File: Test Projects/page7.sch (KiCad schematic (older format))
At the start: 22 parts, among them P2 CONN_01X03, P30 CONN_01X03, U31 SGTL5000, U5 SGTL5000

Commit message: Post review with Byron
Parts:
- added P38, P39: CONN_01X05, Pin_Headers:Pin_Header_Straight_1x05, symbol CONN_01X05
- C10, C11, C12, C13, C14, C37, C38, C39, C40, C41: footprint Capacitors_SMD:C_1206 -> Capacitors_SMD:C_0603
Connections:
- net GND: now also U31.33 (GND), U5.33 (GND), P38.1 (P1), P39.1 (P1)
- net at U5.11 (LINEOUTR): now also P38.4 (P4)
- net at U5.12 (LINEOUTL): now also P38.5 (P5)
- net at U5.13 (LINEINR): now also P38.3 (P3)
- net at U5.14 (LINEINL): now also P38.2 (P2)
- net at U31.11 (LINEOUTR): now also P39.4 (P4)
- net at U31.12 (LINEOUTL): now also P39.5 (P5)
- net at U31.13 (LINEINR): now also P39.3 (P3)
- net at U31.14 (LINEINL): now also P39.2 (P2)

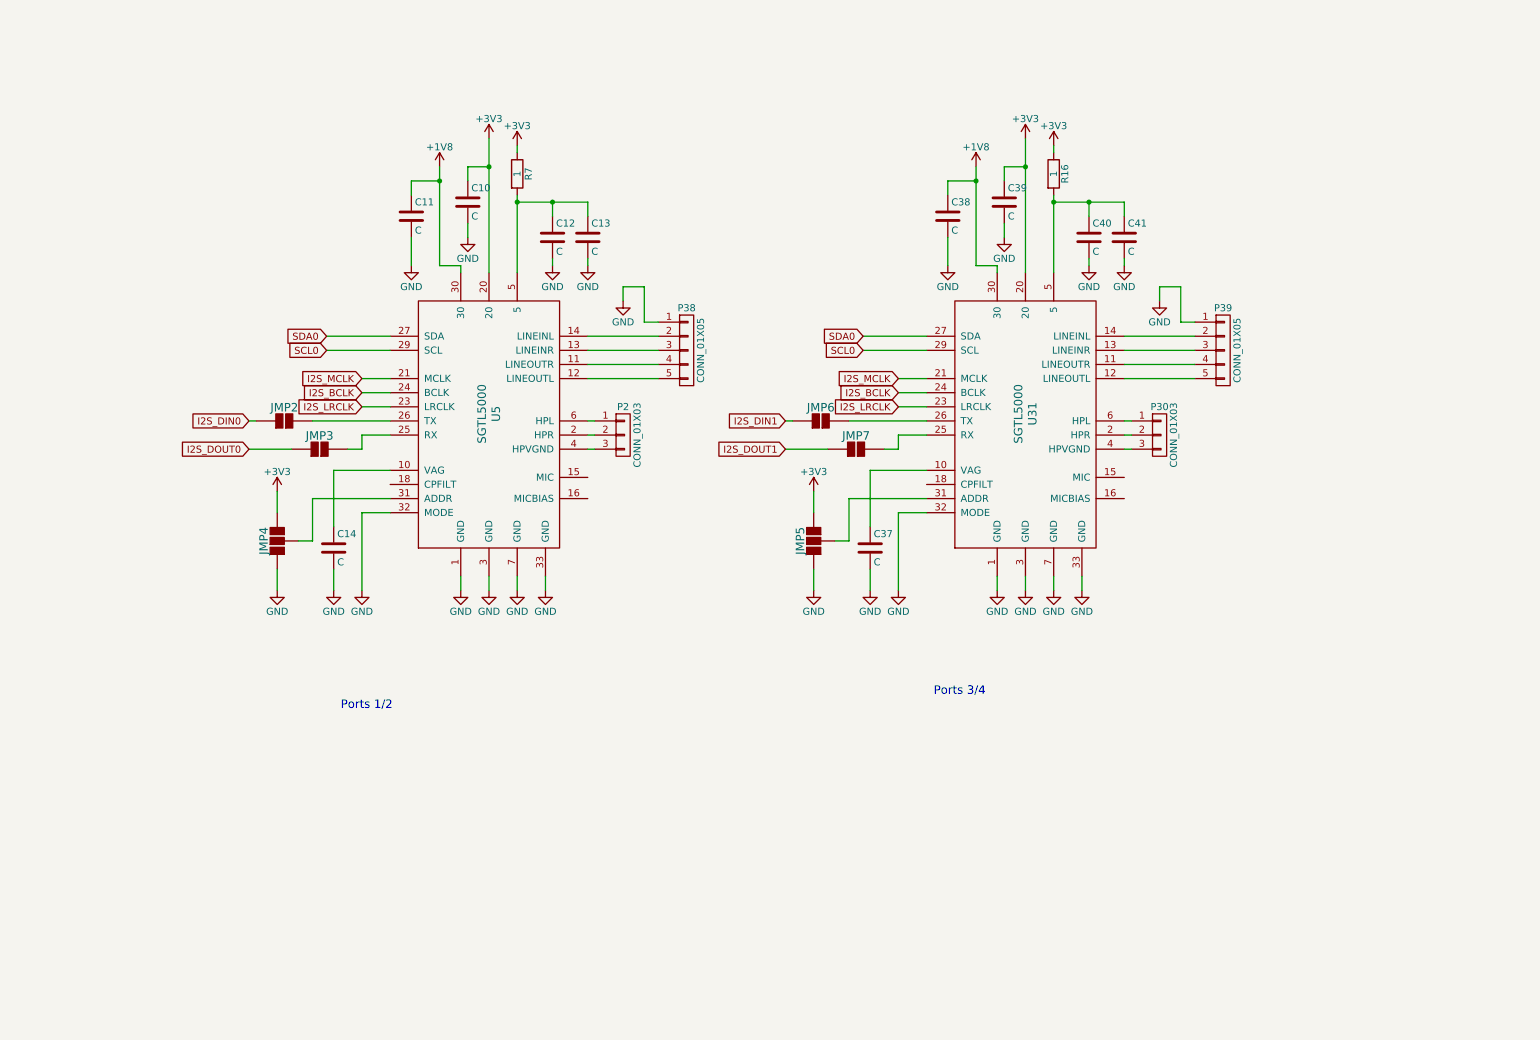
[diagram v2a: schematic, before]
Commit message: Added holes, moved layout
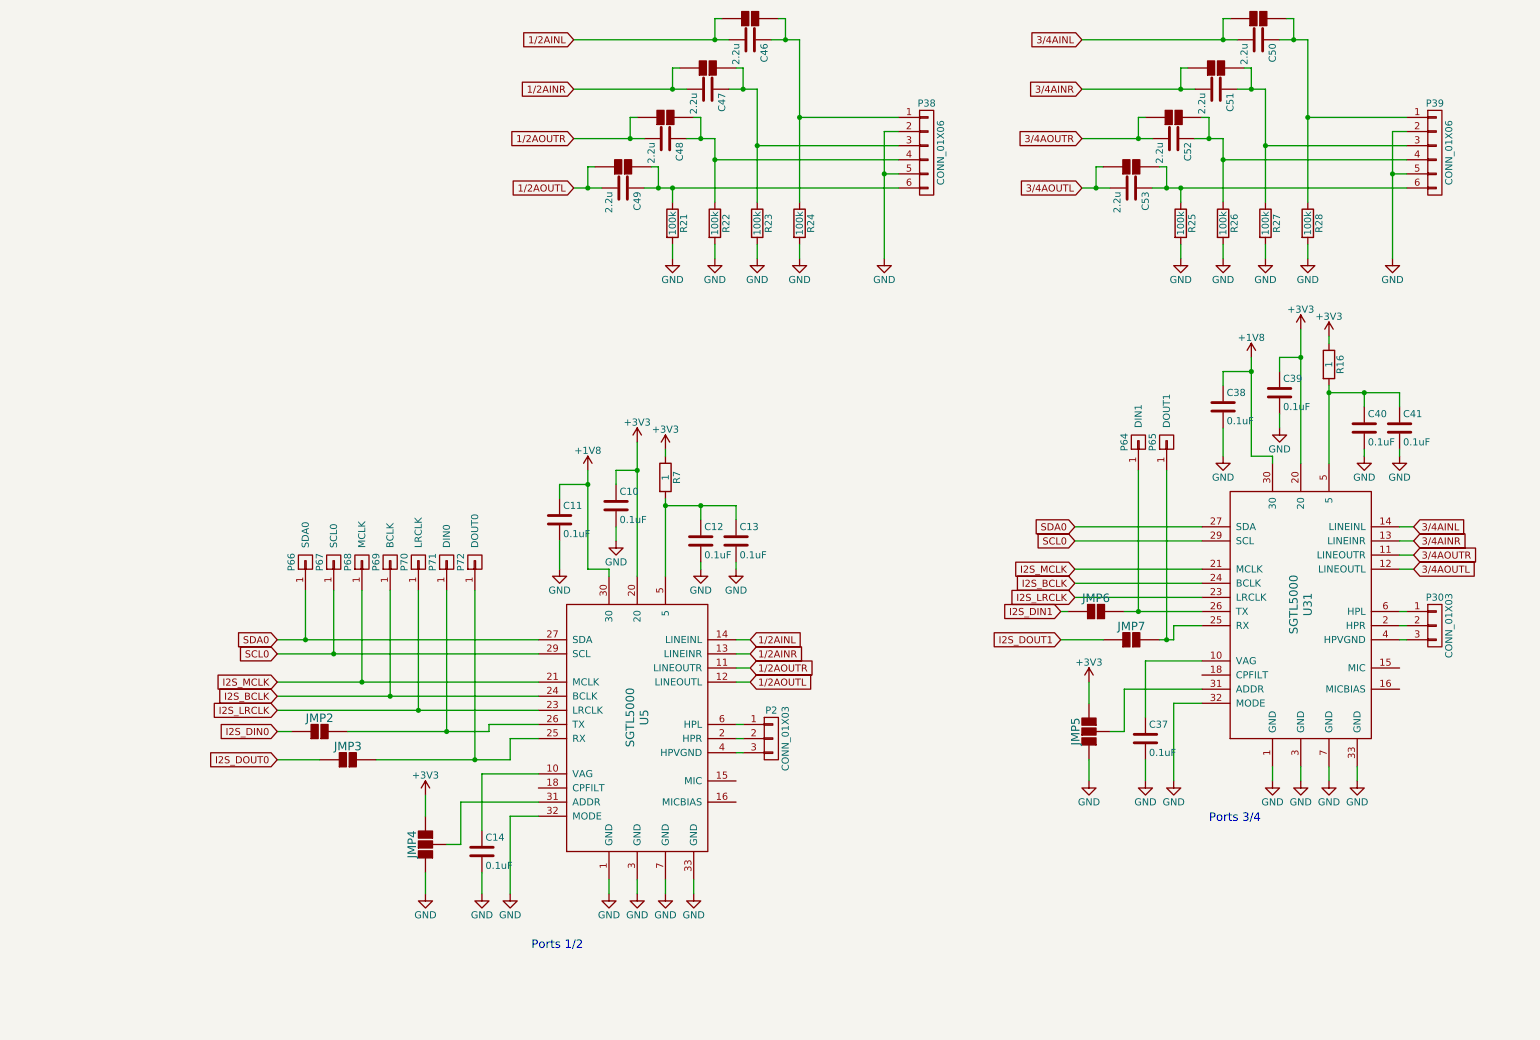
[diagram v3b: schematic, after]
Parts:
- removed P38, P39: CONN_01X05, Pin_Headers:Pin_Header_Straight_1x05, symbol CONN_01X05
- added C46, C47, C48, C49, C50, C51, C52, C53: 2.2u, Capacitors_Tantalum_SMD:TantalC_SizeB_EIA-3528_Reflow, symbol C
- added JMP10, JMP11, JMP12, JMP13, JMP14, JMP15, JMP16, JMP17: 2Jumper, SparkFun-Footprints:SF-2way-open, symbol 2Jumper
- added P38, P39: CONN_01X06, Pin_Headers:Pin_Header_Straight_1x06, symbol CONN_01X06
- added P64: DIN1, SparkFun-Footprints:TestHole, symbol CONN_01X01
- added P65: DOUT1, SparkFun-Footprints:TestHole, symbol CONN_01X01
- added P66: SDA0, SparkFun-Footprints:TestHole, symbol CONN_01X01
- added P67: SCL0, SparkFun-Footprints:TestHole, symbol CONN_01X01
- added P68: MCLK, SparkFun-Footprints:TestHole, symbol CONN_01X01
- added P69: BCLK, SparkFun-Footprints:TestHole, symbol CONN_01X01
- added P70: LRCLK, SparkFun-Footprints:TestHole, symbol CONN_01X01
- added P71: DIN0, SparkFun-Footprints:TestHole, symbol CONN_01X01
- added P72: DOUT0, SparkFun-Footprints:TestHole, symbol CONN_01X01
- added R21, R22, R23, R24, R25, R26, R27, R28: 100k, Resistors_SMD:R_0603, symbol R
- C10, C11, C12, C13, C14, C37, C38, C39, C40, C41: value C -> 0.1uF
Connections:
- net GND: now also P38.2 (P2), P38.5 (P5), P39.2 (P2), P39.5 (P5), R21.2, R22.2, R23.2, R24.2, R25.2, R26.2, R27.2, R28.2
- net I2S_BCLK: now also P69.1 (P1)
- net I2S_LRCLK: now also P70.1 (P1)
- net I2S_MCLK: now also P68.1 (P1)
- net SCL0: now also P67.1 (P1)
- net SDA0: now also P66.1 (P1)
- net at JMP3.2, U5.25 (RX): now also P72.1 (P1)
- net at JMP2.2, U5.26 (TX): now also P71.1 (P1)
- net 1/2AOUTR: now reaches U5.11 (LINEOUTR)
- net 1/2AOUTR: now also C48.2, JMP11.1
- net 1/2AOUTL: now reaches U5.12 (LINEOUTL)
- net 1/2AOUTL: now also C49.2, JMP10.1
- net 1/2AINR: now reaches U5.13 (LINEINR)
- net 1/2AINR: now also C47.2, JMP12.1
- net 1/2AINL: now reaches U5.14 (LINEINL)
- net 1/2AINL: now also C46.2, JMP13.1
- net at JMP7.2, U31.25 (RX): now also P65.1 (P1)
- net at JMP6.2, U31.26 (TX): now also P64.1 (P1)
- net 3/4AOUTR: now reaches U31.11 (LINEOUTR)
- net 3/4AOUTR: now also C52.2, JMP15.1
- net 3/4AOUTL: now reaches U31.12 (LINEOUTL)
- net 3/4AOUTL: now also C53.2, JMP14.1
- net 3/4AINR: now reaches U31.13 (LINEINR)
- net 3/4AINR: now also C51.2, JMP16.1
- net 3/4AINL: now reaches U31.14 (LINEINL)
- net 3/4AINL: now also C50.2, JMP17.1
- new net: C49.1, JMP10.2, P38.6 (P6), R21.1
- new net: C46.1, JMP13.2, P38.1 (P1), R24.1
- new net: C47.1, JMP12.2, P38.3 (P3), R23.1
- new net: C48.1, JMP11.2, P38.4 (P4), R22.1
- new net: C53.1, JMP14.2, P39.6 (P6), R25.1
- new net: C50.1, JMP17.2, P39.1 (P1), R28.1
- new net: C51.1, JMP16.2, P39.3 (P3), R27.1
- new net: C52.1, JMP15.2, P39.4 (P4), R26.1
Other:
- moved on the sheet: C10, C11, C12, C13, C14, C37, C38, C39, C40, C41, JMP2, JMP3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

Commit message: Routing, 15%
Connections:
- net 1/2AOUTL: now also C48.2, JMP11.1; no longer C49.2, JMP10.1
- net 1/2AOUTR: now also C49.2, JMP10.1; no longer C48.2, JMP11.1
- net 3/4AOUTL: now also C52.2, JMP15.1; no longer C53.2, JMP14.1
- net 3/4AOUTR: now also C53.2, JMP14.1; no longer C52.2, JMP15.1
- net I2S_DIN0: now also P71.1 (P1)
- net I2S_DIN1: now also P64.1 (P1)
- net I2S_DOUT0: now also P72.1 (P1)
- net I2S_DOUT1: now also P65.1 (P1)
- net at JMP3.2, U5.25 (RX): no longer P72.1 (P1)
- net at JMP2.2, U5.26 (TX): no longer P71.1 (P1)
- net at JMP7.2, U31.25 (RX): no longer P65.1 (P1)
- net at JMP6.2, U31.26 (TX): no longer P64.1 (P1)
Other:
- moved on the sheet: JMP2, JMP3, P64, P65, P66, P67, P68, P69, P70, P71, P72
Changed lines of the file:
@@
 EESchema Schematic File Version 2
+LIBS:Teensy_test_layout-rescue
 LIBS:power
 LIBS:device
@@
 LIBS:SparkFun-Mounting
 LIBS:SparkFun-Opto
+LIBS:SparkFun-Connectors
 LIBS:Teensy_test_layout-cache
 EELAYER 25 0
@@
 L 2Jumper JMP3
 U 1 1 569EDBC7
-P 2800 5800
-F 0 "JMP3" H 2800 5895 60  0000 C CNN
-F 1 "2Jumper" H 2800 5985 60  0001 C CNN
-F 2 "SparkFun-Footprints:SF-2way-open" H 3955 5870 60  0001 C CNN
-F 3 "" H 3955 5870 60  0000 C CNN
-	1    2800 5800
+P 3300 5800
+F 0 "JMP3" H 3300 5895 60  0000 C CNN
+F 1 "2Jumper" H 3300 5985 60  0001 C CNN
+F 2 "SparkFun-Footprints:SF-2way-open" H 4455 5870 60  0001 C CNN
+F 3 "" H 4455 5870 60  0000 C CNN
+	1    3300 5800
 	1    0    0    -1
 $EndComp
@@
 L 2Jumper JMP2
 U 1 1 569EDBD5
-P 2600 5600
-F 0 "JMP2" H 2600 5695 60  0000 C CNN
-F 1 "2Jumper" H 2600 5785 60  0001 C CNN
-F 2 "SparkFun-Footprints:SF-2way-open" H 3755 5670 60  0001 C CNN
-F 3 "" H 3755 5670 60  0000 C CNN
-	1    2600 5600
+P 3100 5600
+F 0 "JMP2" H 3100 5695 60  0000 C CNN
+F 1 "2Jumper" H 3100 5785 60  0001 C CNN
+F 2 "SparkFun-Footprints:SF-2way-open" H 4255 5670 60  0001 C CNN
+F 3 "" H 4255 5670 60  0000 C CNN
+	1    3100 5600
 	1    0    0    -1
 $EndComp
@@
 	2300 4950 4150 4950
 Wire Wire Line
-	2400 5600 2300 5600
-Wire Wire Line
-	2600 5800 2300 5800
+	2300 5600 2900 5600
+Wire Wire Line
+	2300 5800 3100 5800
 Wire Wire Line
 	4850 3550 4850 4500
@@
 	1    0    0    -1
 $EndComp
-Text GLabel 7950 4150 0    50   Input ~ 0
+Text GLabel 7150 4150 0    50   Input ~ 0
 SDA0
-Text GLabel 7950 4250 0    50   Input ~ 0
+Text GLabel 7150 4250 0    50   Input ~ 0
 SCL0
-Text GLabel 7950 4450 0    50   Input ~ 0
+Text GLabel 7150 4450 0    50   Input ~ 0
 I2S_MCLK
-Text GLabel 7950 4550 0    50   Input ~ 0
+Text GLabel 7150 4550 0    50   Input ~ 0
 I2S_BCLK
-Text GLabel 7950 4650 0    50   Input ~ 0
+Text GLabel 7150 4650 0    50   Input ~ 0
 I2S_LRCLK
-Text GLabel 7850 4750 0    50   Input ~ 0
+Text GLabel 7050 4750 0    50   Input ~ 0
 I2S_DIN1
-Text GLabel 7850 4950 0    50   Input ~ 0
+Text GLabel 7050 4950 0    50   Input ~ 0
 I2S_DOUT1
 $Comp
@@
 	8650 4850 8850 4850
 Wire Wire Line
-	8850 4650 7950 4650
-Wire Wire Line
-	8850 4550 7950 4550
-Wire Wire Line
-	8850 4450 7950 4450
-Wire Wire Line
-	7950 4250 8850 4250
-Wire Wire Line
-	7950 4150 8850 4150
-Wire Wire Line
-	7900 4750 7850 4750
-Wire Wire Line
-	8150 4950 7850 4950
+	8850 4650 7150 4650
+Wire Wire Line
+	8850 4550 7150 4550
+Wire Wire Line
+	8850 4450 7150 4450
+Wire Wire Line
+	7150 4250 8850 4250
+Wire Wire Line
+	7150 4150 8850 4150
+Wire Wire Line
+	7050 4750 7900 4750
+Wire Wire Line
+	7050 4950 8150 4950
 Wire Wire Line
 	9550 2750 9550 3700
@@
 Text GLabel 4400 1050 0    50   Input ~ 0
 1/2AINR
+Text GLabel 4400 1750 0    50   Input ~ 0
+1/2AOUTR
 Text GLabel 4400 1400 0    50   Input ~ 0
-1/2AOUTR
-Text GLabel 4400 1750 0    50   Input ~ 0
 1/2AOUTL
 Wire Wire Line
@@
 Text GLabel 8000 1050 0    50   Input ~ 0
 3/4AINR
+Text GLabel 8000 1750 0    50   Input ~ 0
+3/4AOUTR
 Text GLabel 8000 1400 0    50   Input ~ 0
-3/4AOUTR
-Text GLabel 8000 1750 0    50   Input ~ 0
 3/4AOUTL
 Wire Wire Line
-	2800 5600 3800 5600
+	3300 5600 3800 5600
 Wire Wire Line
 	3800 5600 3800 5550
@@
 	3800 5550 4150 5550
 Wire Wire Line
-	3000 5800 3950 5800
+	3500 5800 3950 5800
 $Comp
 L CONN_01X01 P72
 U 1 1 56A4747C
+P 2700 4400
+F 0 "P72" H 2700 4500 50  0000 C CNN
+F 1 "DOUT0" H 2800 4400 50  0000 L CNN
+F 2 "SparkFun-Footprints:TestHole" H 2700 4400 50  0001 C CNN
+F 3 "" H 2700 4400 50  0000 C CNN
+	1    2700 4400
+	0    -1   -1   0
+$EndComp
+$Comp
+L CONN_01X01 P71
+U 1 1 56A47876
+P 2500 4400
+F 0 "P71" H 2500 4500 50  0000 C CNN
+F 1 "DIN0" H 2600 4400 50  0000 L CNN
+F 2 "SparkFun-Footprints:TestHole" H 2500 4400 50  0001 C CNN
+F 3 "" H 2500 4400 50  0000 C CNN
+	1    2500 4400
+	0    -1   -1   0
+$EndComp
+$Comp
+L CONN_01X01 P70
+U 1 1 56A47910
 P 3700 4400
-F 0 "P72" H 3700 4500 50  0000 C CNN
-F 1 "DOUT0" H 3800 4400 50  0000 L CNN
+F 0 "P70" H 3700 4500 50  0000 C CNN
+F 1 "LRCLK" H 3800 4400 50  0000 L CNN
 F 2 "SparkFun-Footprints:TestHole" H 3700 4400 50  0001 C CNN
 F 3 "" H 3700 4400 50  0000 C CNN
@@
 $EndComp
 $Comp
-L CONN_01X01 P71
-U 1 1 56A47876
+L CONN_01X01 P69
+U 1 1 56A479A5
 P 3500 4400
-F 0 "P71" H 3500 4500 50  0000 C CNN
-F 1 "DIN0" H 3600 4400 50  0000 L CNN
+F 0 "P69" H 3500 4500 50  0000 C CNN
+F 1 "BCLK" H 3600 4400 50  0000 L CNN
 F 2 "SparkFun-Footprints:TestHole" H 3500 4400 50  0001 C CNN
 F 3 "" H 3500 4400 50  0000 C CNN
@@
 $EndComp
 $Comp
-L CONN_01X01 P70
-U 1 1 56A47910
+L CONN_01X01 P68
+U 1 1 56A47A41
 P 3300 4400
-F 0 "P70" H 3300 4500 50  0000 C CNN
-F 1 "LRCLK" H 3400 4400 50  0000 L CNN
+F 0 "P68" H 3300 4500 50  0000 C CNN
+F 1 "MCLK" H 3400 4400 50  0000 L CNN
 F 2 "SparkFun-Footprints:TestHole" H 3300 4400 50  0001 C CNN
 F 3 "" H 3300 4400 50  0000 C CNN
@@
 $EndComp
 $Comp
-L CONN_01X01 P69
-U 1 1 56A479A5
+L CONN_01X01 P67
+U 1 1 56A47ADC
 P 3100 4400
-F 0 "P69" H 3100 4500 50  0000 C CNN
-F 1 "BCLK" H 3200 4400 50  0000 L CNN
+F 0 "P67" H 3100 4500 50  0000 C CNN
+F 1 "SCL0" H 3200 4400 50  0000 L CNN
 F 2 "SparkFun-Footprints:TestHole" H 3100 4400 50  0001 C CNN
 F 3 "" H 3100 4400 50  0000 C CNN
@@
 $EndComp
 $Comp
-L CONN_01X01 P68
-U 1 1 56A47A41
+L CONN_01X01 P66
+U 1 1 56A47B7C
 P 2900 4400
-F 0 "P68" H 2900 4500 50  0000 C CNN
-F 1 "MCLK" H 3000 4400 50  0000 L CNN
+F 0 "P66" H 2900 4500 50  0000 C CNN
+F 1 "SDA0" H 3000 4400 50  0000 L CNN
 F 2 "SparkFun-Footprints:TestHole" H 2900 4400 50  0001 C CNN
 F 3 "" H 2900 4400 50  0000 C CNN
@@
 	0    -1   -1   0
 $EndComp
-$Comp
-L CONN_01X01 P67
-U 1 1 56A47ADC
-P 2700 4400
-F 0 "P67" H 2700 4500 50  0000 C CNN
-F 1 "SCL0" H 2800 4400 50  0000 L CNN
-F 2 "SparkFun-Footprints:TestHole" H 2700 4400 50  0001 C CNN
-F 3 "" H 2700 4400 50  0000 C CNN
-	1    2700 4400
-	0    -1   -1   0
-$EndComp
-$Comp
-L CONN_01X01 P66
-U 1 1 56A47B7C
-P 2500 4400
-F 0 "P66" H 2500 4500 50  0000 C CNN
-F 1 "SDA0" H 2600 4400 50  0000 L CNN
-F 2 "SparkFun-Footprints:TestHole" H 2500 4400 50  0001 C CNN
-F 3 "" H 2500 4400 50  0000 C CNN
-	1    2500 4400
-	0    -1   -1   0
-$EndComp
-Wire Wire Line
-	2500 4950 2500 4600
-Connection ~ 2500 4950
-Wire Wire Line
-	2700 4600 2700 5050
-Connection ~ 2700 5050
-Wire Wire Line
-	2900 4600 2900 5250
-Connection ~ 2900 5250
-Wire Wire Line
-	3100 4600 3100 5350
-Connection ~ 3100 5350
-Wire Wire Line
-	3300 4600 3300 5450
-Connection ~ 3300 5450
-Wire Wire Line
-	3500 4600 3500 5600
-Connection ~ 3500 5600
-Wire Wire Line
-	3700 4600 3700 5800
-Connection ~ 3700 5800
+Wire Wire Line
+	2900 4950 2900 4600
+Connection ~ 2900 4950
+Wire Wire Line
+	3100 4600 3100 5050
+Connection ~ 3100 5050
+Wire Wire Line
+	3300 4600 3300 5250
+Connection ~ 3300 5250
+Wire Wire Line
+	3500 4600 3500 5350
+Connection ~ 3500 5350
+Wire Wire Line
+	3700 4600 3700 5450
+Connection ~ 3700 5450
+Wire Wire Line
+	2500 4600 2500 5600
+Wire Wire Line
+	2700 4600 2700 5800
 $Comp
 L CONN_01X01 P65
 U 1 1 56A48D54
-P 8600 3550
-F 0 "P65" H 8600 3650 50  0000 C CNN
-F 1 "DOUT1" H 8700 3550 50  0000 L CNN
-F 2 "SparkFun-Footprints:TestHole" H 8600 3550 50  0001 C CNN
-F 3 "" H 8600 3550 50  0000 C CNN
-	1    8600 3550
+P 7750 3550
+F 0 "P65" H 7750 3650 50  0000 C CNN
+F 1 "DOUT1" H 7850 3550 50  0000 L CNN
+F 2 "SparkFun-Footprints:TestHole" H 7750 3550 50  0001 C CNN
+F 3 "" H 7750 3550 50  0000 C CNN
+	1    7750 3550
 	0    -1   -1   0
 $EndComp
@@
 L CONN_01X01 P64
 U 1 1 56A48D5A
-P 8400 3550
-F 0 "P64" H 8400 3650 50  0000 C CNN
-F 1 "DIN1" H 8500 3550 50  0000 L CNN
-F 2 "SparkFun-Footprints:TestHole" H 8400 3550 50  0001 C CNN
-F 3 "" H 8400 3550 50  0000 C CNN
-	1    8400 3550
+P 7550 3550
+F 0 "P64" H 7550 3650 50  0000 C CNN
+F 1 "DIN1" H 7650 3550 50  0000 L CNN
+F 2 "SparkFun-Footprints:TestHole" H 7550 3550 50  0001 C CNN
+F 3 "" H 7550 3550 50  0000 C CNN
+	1    7550 3550
 	0    -1   -1   0
 $EndComp
 Wire Wire Line
-	8400 3750 8400 4750
-Wire Wire Line
-	8600 3750 8600 4950
-Connection ~ 8600 4950
-Connection ~ 8400 4750
+	7550 3750 7550 4750
+Wire Wire Line
+	7750 3750 7750 4950
 $Comp
 L 2Jumper JMP12
@@
 	8600 1600 8550 1600
 Connection ~ 8600 1750
+Connection ~ 2500 5600
+Connection ~ 2700 5800
+Connection ~ 7550 4750
+Connection ~ 7750 4950
 $EndSCHEMATC

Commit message: moar layout
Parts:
- added JMP22, JMP23, JMP24, JMP25, JMP26: 2Jumper, SparkFun-Footprints:SF-2way-open, symbol 2Jumper
- added P91: SDA0, SparkFun-Footprints:TestHole, symbol CONN_01X01
- added P92: SCL0, SparkFun-Footprints:TestHole, symbol CONN_01X01
- added P93: MCLK, SparkFun-Footprints:TestHole, symbol CONN_01X01
- added P94: BCLK, SparkFun-Footprints:TestHole, symbol CONN_01X01
- added P95: LRCLK, SparkFun-Footprints:TestHole, symbol CONN_01X01
- added P96: DIN1_ISO, SparkFun-Footprints:TestHole, symbol CONN_01X01
- added P97: DOUT1_ISO, SparkFun-Footprints:TestHole, symbol CONN_01X01
- added P98: DIN0_ISO, SparkFun-Footprints:TestHole, symbol CONN_01X01
- added P99: DOUT0_ISO, SparkFun-Footprints:TestHole, symbol CONN_01X01
- P66: value SDA0 -> SDA0_ISO
- P67: value SCL0 -> SCL0_ISO
- P68: value MCLK -> MCLK_ISO
- P69: value BCLK -> BCLK_ISO
- P70: value LRCLK -> LRCLK_ISO
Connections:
- net I2S_BCLK: now also JMP25.1, P94.1 (P1); no longer P69.1 (P1), U31.24 (BCLK), U5.24 (BCLK)
- net I2S_LRCLK: now also JMP26.1, P95.1 (P1); no longer P70.1 (P1), U31.23 (LRCLK), U5.23 (LRCLK)
- net I2S_MCLK: now also JMP24.1, P93.1 (P1); no longer P68.1 (P1), U31.21 (MCLK), U5.21 (MCLK)
- net SCL0: now also JMP23.1, P92.1 (P1); no longer P67.1 (P1), U31.29 (SCL), U5.29 (SCL)
- net SDA0: now also JMP22.1, P91.1 (P1); no longer P66.1 (P1), U31.27 (SDA), U5.27 (SDA)
- net I2S_DOUT0_ISO: now reaches JMP3.2, U5.25 (RX)
- net I2S_DOUT0_ISO: now also P99.1 (P1)
- net I2S_DIN0_ISO: now reaches JMP2.2, U5.26 (TX)
- net I2S_DIN0_ISO: now also P98.1 (P1)
- net I2S_DOUT1_ISO: now reaches JMP7.2, U31.25 (RX)
- net I2S_DOUT1_ISO: now also P97.1 (P1)
- net I2S_DIN1_ISO: now reaches JMP6.2, U31.26 (TX)
- net I2S_DIN1_ISO: now also P96.1 (P1)
- new net BCLK_ISO: JMP25.2, P69.1 (P1), U31.24 (BCLK), U5.24 (BCLK)
- new net LRCLK_ISO: JMP26.2, P70.1 (P1), U31.23 (LRCLK), U5.23 (LRCLK)
- new net MCLK_ISO: JMP24.2, P68.1 (P1), U31.21 (MCLK), U5.21 (MCLK)
- new net SCL_ISO: JMP23.2, P67.1 (P1), U31.29 (SCL), U5.29 (SCL)
- new net SDA_ISO: JMP22.2, P66.1 (P1), U31.27 (SDA), U5.27 (SDA)
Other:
- moved on the sheet: JMP2, JMP3, JMP6, JMP7, P64, P65, P66, P67, P68, P69, P70, P71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

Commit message: layout
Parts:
- added JMP27, JMP28: 2Jumper, SparkFun-Footprints:SF-2way-open, symbol 2Jumper
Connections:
- net GND: now also JMP27.1, JMP28.1; no longer C10.2, C11.2, C12.2, C13.2, C14.2, C37.2, C38.2, C39.2, C40.2, C41.2, JMP4.1, JMP5.1, P38.2 (P2), P38.5 (P5), P39.2 (P2), P39.5 (P5), R21.2, R22.2, R23.2, R24.2, R25.2, R26.2, R27.2, R28.2, U31.1 (GND), U31.3 (GND), U31.32 (MODE), U31.33 (GND), U31.7 (GND), U5.1 (GND), U5.3 (GND), U5.32 (MODE), U5.33 (GND), U5.7 (GND)
- new net ISOGND12: C10.2, C11.2, C12.2, C13.2, C14.2, JMP27.2, JMP4.1, P38.2 (P2), P38.5 (P5), R21.2, R22.2, R23.2, R24.2, U5.1 (GND), U5.3 (GND), U5.32 (MODE), U5.33 (GND), U5.7 (GND)
- new net ISOGND34: C37.2, C38.2, C39.2, C40.2, C41.2, JMP28.2, JMP5.1, P39.2 (P2), P39.5 (P5), R25.2, R26.2, R27.2, R28.2, U31.1 (GND), U31.3 (GND), U31.32 (MODE), U31.33 (GND), U31.7 (GND)
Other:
- moved on the sheet: C12, C13, C40, C41
